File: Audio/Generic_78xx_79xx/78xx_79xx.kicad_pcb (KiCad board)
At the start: 2 copper layers, 48.3 x 76.2 mm, 13 parts, among them P1 CONN_01X03, P2 CONN_01X02, P3 CONN_01X02, U1 LM7812CT, U2 LM7912CT

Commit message: Further revision
More fixes
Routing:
- net +Vin: track 42.8 -> 41.6 mm
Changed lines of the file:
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@@
-(kicad_pcb (version 4) (host pcbnew 4.0.0-rc2-stable)
+(kicad_pcb (version 4) (host pcbnew 4.0.0-stable)
   (general
     (links 24)
@@
     (thickness 1.6)
     (drawings 6)
-    (tracks 72)
+    (tracks 70)
     (zones 0)
     (modules 13)
@@
     (arrow2b (pts (xy 71.12 17.78) (xy 72.246504 17.193579)))
   )
+  (segment (start 78.74 60.96) (end 81.28 63.5) (width 1.75) (layer B.Cu) (net 1))
+  (segment (start 81.28 63.5) (end 82.55 64.77) (width 1.75) (layer B.Cu) (net 1))
+  (segment (start 85.09 62.23) (end 82.55 64.77) (width 1.75) (layer B.Cu) (net 1))
+  (segment (start 82.55 64.77) (end 82.55 66.04) (width 1.75) (layer B.Cu) (net 1))
   (segment (start 82.55 76.2) (end 82.55 82.55) (width 1.75) (layer B.Cu) (net 1))
   (segment (start 82.55 82.55) (end 87.63 87.63) (width 1.75) (layer B.Cu) (net 1))
   (segment (start 87.63 87.63) (end 95.25 87.63) (width 1.75) (layer B.Cu) (net 1))
-  (segment (start 82.55 66.04) (end 78.74 62.23) (width 1.75) (layer B.Cu) (net 1))
-  (segment (start 78.74 62.23) (end 78.74 60.96) (width 1.75) (layer B.Cu) (net 1))
-  (segment (start 85.09 63.5) (end 85.09 62.23) (width 1.75) (layer B.Cu) (net 1))
-  (segment (start 82.55 66.04) (end 85.09 63.5) (width 1.75) (layer B.Cu) (net 1))
   (segment (start 82.55 76.2) (end 82.55 66.04) (width 1.75) (layer B.Cu) (net 1))
   (segment (start 100.33 54.61) (end 95.25 54.61) (width 1.75) (layer B.Cu) (net 2))
@@
   (segment (start 105.33 54.61) (end 106.68 54.61) (width 1.75) (layer B.Cu) (net 4))
   (segment (start 106.68 54.61) (end 107.95 55.88) (width 1.75) (layer B.Cu) (net 4))
+  (segment (start 107.83 40.64) (end 107.83 45.72) (width 1.75) (layer B.Cu) (net 5))
+  (segment (start 107.83 45.72) (end 107.95 45.72) (width 1.75) (layer B.Cu) (net 5))
+  (segment (start 107.95 45.72) (end 116.84 54.61) (width 1.75) (layer B.Cu) (net 5))
+  (segment (start 116.84 54.61) (end 116.84 58.42) (width 1.75) (layer B.Cu) (net 5))
+  (segment (start 116.84 58.42) (end 114.3 60.96) (width 1.75) (layer B.Cu) (net 5))
+  (segment (start 114.3 60.96) (end 111.76 60.96) (width 1.75) (layer B.Cu) (net 5))
+  (segment (start 110.49 62.23) (end 111.76 60.96) (width 1.75) (layer B.Cu) (net 5))
+  (segment (start 105.33 62.23) (end 110.49 62.23) (width 1.75) (layer B.Cu) (net 5))
   (segment (start 107.83 40.64) (end 107.83 32.18251) (width 1.75) (layer B.Cu) (net 5))
   (segment (start 107.83 32.18251) (end 104.85749 29.21) (width 1.75) (layer B.Cu) (net 5))
   (segment (start 104.85749 29.21) (end 101.6 29.21) (width 1.75) (layer B.Cu) (net 5))
   (segment (start 88.9 29.21) (end 101.6 29.21) (width 1.75) (layer B.Cu) (net 5))
-  (segment (start 107.83 40.64) (end 107.83 46.87) (width 1.75) (layer B.Cu) (net 5))
-  (segment (start 107.83 46.87) (end 110.49 49.53) (width 1.75) (layer B.Cu) (net 5))
-  (segment (start 110.49 49.53) (end 113.03 49.53) (width 1.75) (layer B.Cu) (net 5))
-  (segment (start 113.03 49.53) (end 115.57 52.07) (width 1.75) (layer B.Cu) (net 5))
-  (segment (start 115.57 52.07) (end 115.57 59.69) (width 1.75) (layer B.Cu) (net 5))
-  (segment (start 115.57 59.69) (end 114.3 60.96) (width 1.75) (layer B.Cu) (net 5))
-  (segment (start 114.3 60.96) (end 111.76 60.96) (width 1.75) (layer B.Cu) (net 5))
   (segment (start 111.76 60.96) (end 113.03 60.96) (width 1.75) (layer B.Cu) (net 5))
-  (segment (start 107.95 60.96) (end 111.76 60.96) (width 1.75) (layer B.Cu) (net 5))
-  (segment (start 106.68 62.23) (end 107.95 60.96) (width 1.75) (layer B.Cu) (net 5))
-  (segment (start 105.33 62.23) (end 106.68 62.23) (width 1.75) (layer B.Cu) (net 5))
 )

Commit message: Improvements
PCB revised.
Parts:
- moved P3 7.41 mm to (95.2, 31.8), turned to 0 degrees
- moved P2 6.48 mm to (95.2, 26.7), turned to 0 degrees
- moved C4 6.35 mm to (86.4, 45.7), turned to 90 degrees
- moved C8 4.58 mm to (104.1, 38.1), turned to 270 degrees
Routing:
- net GND: track 121.0 -> 147.3 mm
- net +Vreg: track 54.2 -> 47.7 mm
- net -Vreg: track 64.6 -> 62.3 mm

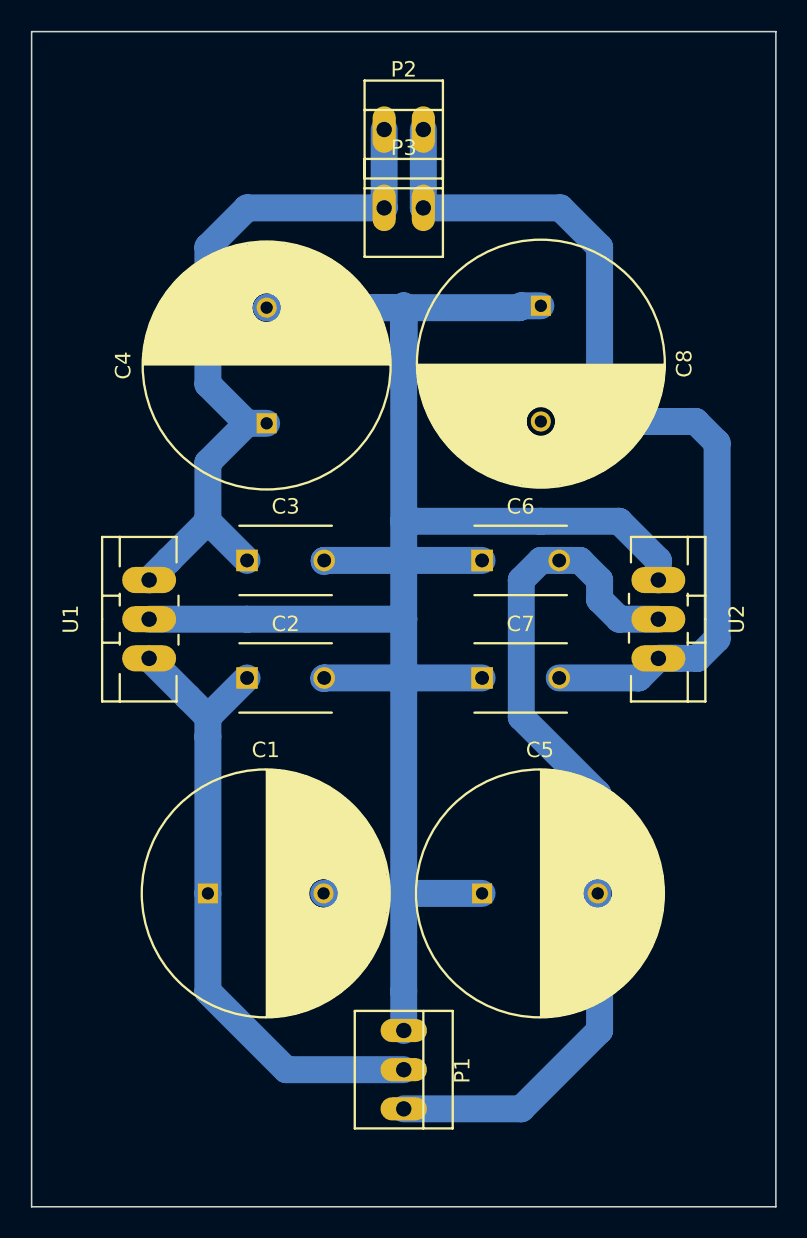
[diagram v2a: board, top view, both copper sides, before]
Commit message: Fixes for SSM2142(PCB)
Reworked for smaller footprint of PCB.
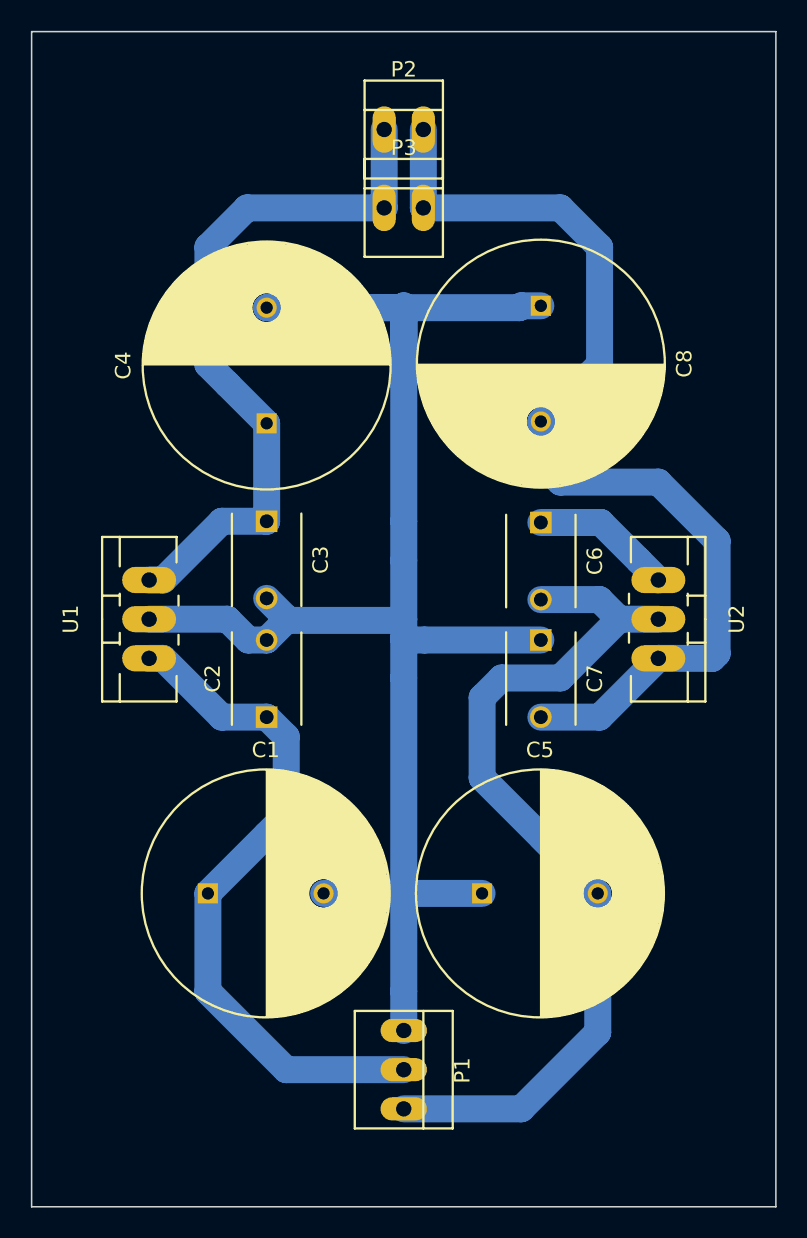
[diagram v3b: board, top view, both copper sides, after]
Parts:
- moved C6 4.54 mm to (104.1, 52.1), turned to 270 degrees
- moved C7 4.54 mm to (104.1, 59.8), turned to 270 degrees
- moved C2 2.84 mm to (86.4, 64.8), turned to 90 degrees
- moved C3 2.84 mm to (86.4, 52.1), turned to 270 degrees
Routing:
- net GND: track 147.3 -> 129.0 mm
- net -Vreg: track 62.3 -> 67.2 mm
- net +Vin: track 41.6 -> 44.4 mm
- net +Vreg: track 47.7 -> 46.1 mm
- net -Vin: track 59.1 -> 60.4 mm
